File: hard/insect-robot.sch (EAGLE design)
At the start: 9 parts, among them Q1 AO3400, SW1 MK-12C02, U1 ATMEGA328P-QFN32, U2 PW0316

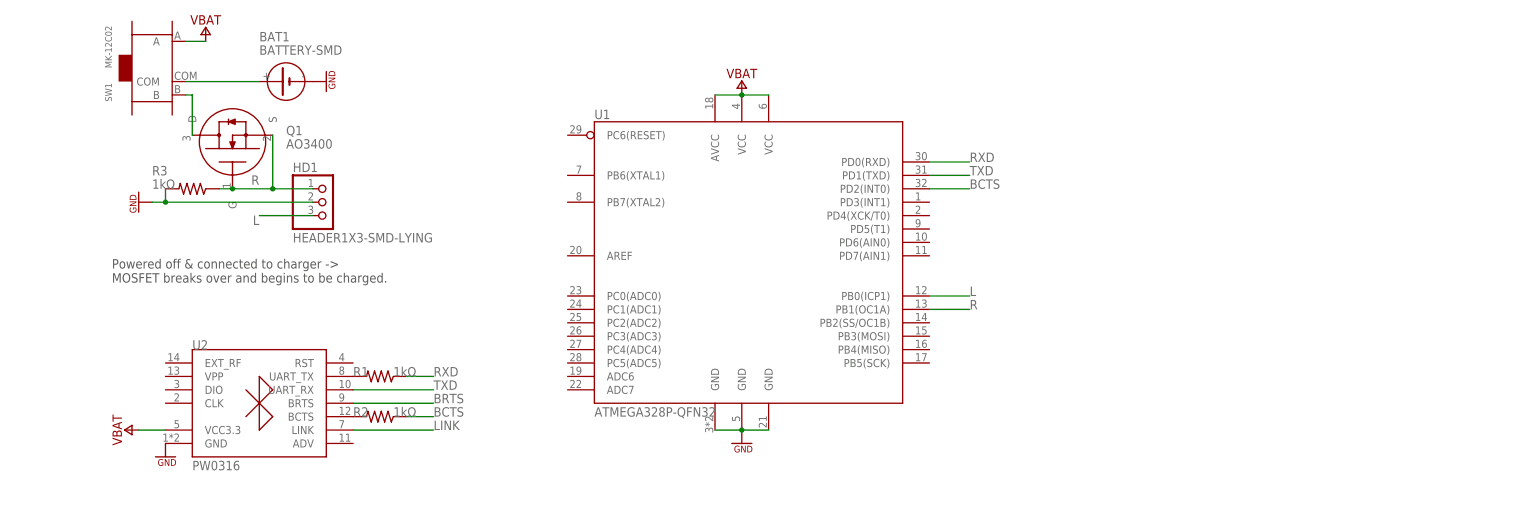
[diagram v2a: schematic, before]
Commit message: Add ISP programming port
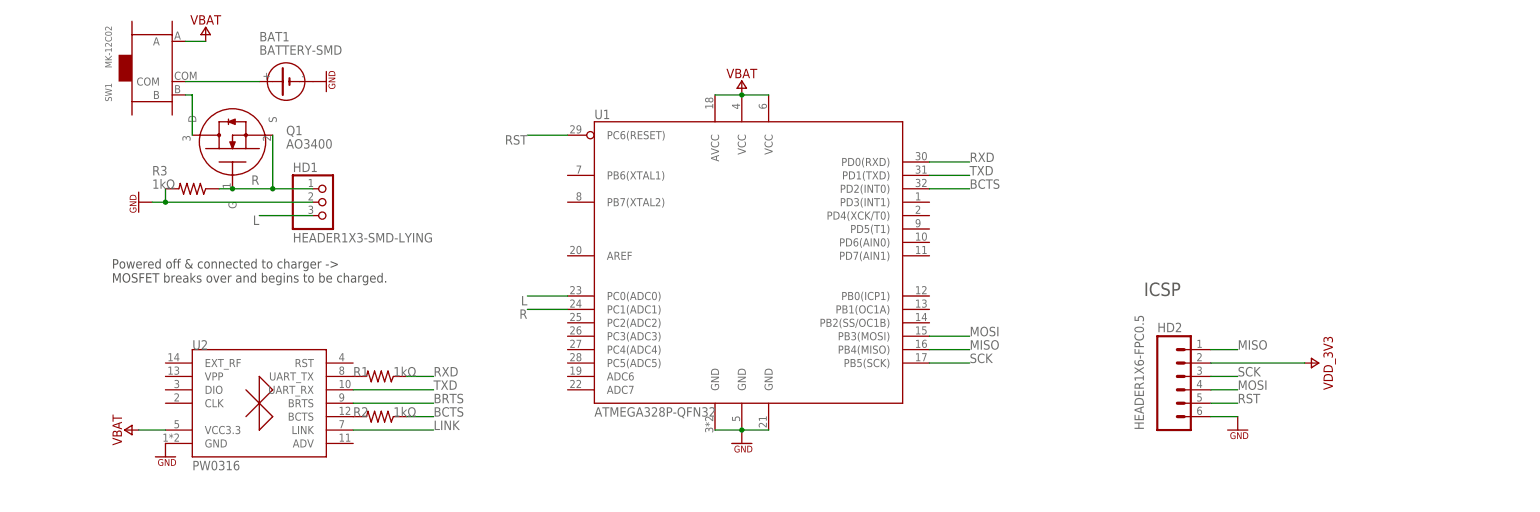
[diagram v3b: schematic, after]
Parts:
- added HD2: HEADER1X6-FPC0.5, MyLibrary:HEADER1X6-FPC0.5
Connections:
- net N$1 renamed SWITCH-B
- new net MISO: HD2.1, U1.PB4(MISO)
- new net MOSI: HD2.4, U1.PB3(MOSI)
- new net RST: HD2.5, U1.PC6(RESET)
- new net SCK: HD2.3, U1.PB5(SCK)
- new net VDD_3V3: HD2.2
- net GND: now also HD2.6
- net L: now also U1.PC0(ADC0); no longer U1.PB0(ICP1)
- net R: now also U1.PC1(ADC1); no longer U1.PB1(OC1A)
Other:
- note added: "ICSP"
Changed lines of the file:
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@@
 <part name="Q1" library="MyLibrary" deviceset="MOSFET" device="-SOT23" value="AO3400"/>
 <part name="R3" library="MyLibrary" deviceset="RES" device="-0603" value="1kΩ"/>
+<part name="HD2" library="MyLibrary" deviceset="HEADER1X6" device="-FPC0.5"/>
+<part name="SUPPLY25" library="MyLibrary" deviceset="GND" device=""/>
+<part name="SUPPLY26" library="MyLibrary" deviceset="VDD_3V3" device=""/>
 </parts>
 <sheets>
@@
 <text x="-119.38" y="-2.54" size="1.778" layer="97">Powered off &amp; connected to charger -&gt;
 MOSFET breaks over and begins to be charged.</text>
+<text x="76.2" y="-5.08" size="2.54" layer="97" font="vector">ICSP</text>
 </plain>
 <instances>
@@
 <attribute name="VALUE" x="-111.76" y="15.24" size="1.778" layer="96"/>
 </instance>
+<instance part="HD2" gate="A" x="83.82" y="-22.86" smashed="yes">
+<attribute name="VALUE" x="76.2" y="-30.48" size="1.778" layer="96" rot="R90"/>
+<attribute name="NAME" x="78.74" y="-11.938" size="1.778" layer="95"/>
+</instance>
+<instance part="SUPPLY25" gate="GND" x="93.98" y="-30.48"/>
+<instance part="SUPPLY26" gate="VDD_3V3" x="109.22" y="-17.78" rot="R270"/>
 </instances>
 <busses>
@@
 <pinref part="U2" gate="P" pin="GND"/>
 <pinref part="SUPPLY7" gate="GND" pin="GND"/>
+</segment>
+<segment>
+<pinref part="HD2" gate="A" pin="6"/>
+<wire x1="88.9" y1="-27.94" x2="93.98" y2="-27.94" width="0.1524" layer="91"/>
+<pinref part="SUPPLY25" gate="GND" pin="GND"/>
 </segment>
 </net>
@@
 </segment>
 <segment>
-<pinref part="U1" gate="P" pin="PB1(OC1A)"/>
-<wire x1="35.56" y1="-7.62" x2="43.18" y2="-7.62" width="0.1524" layer="91"/>
-<label x="43.18" y="-7.62" size="1.778" layer="95" font="vector"/>
+<pinref part="U1" gate="P" pin="PC1(ADC1)"/>
+<wire x1="-33.02" y1="-7.62" x2="-40.64" y2="-7.62" width="0.1524" layer="91"/>
+<label x="-40.64" y="-7.62" size="1.778" layer="95" font="vector" rot="R180"/>
 </segment>
 </net>
@@
 </segment>
 <segment>
-<pinref part="U1" gate="P" pin="PB0(ICP1)"/>
-<wire x1="35.56" y1="-5.08" x2="43.18" y2="-5.08" width="0.1524" layer="91"/>
-<label x="43.18" y="-5.08" size="1.778" layer="95" font="vector"/>
+<pinref part="U1" gate="P" pin="PC0(ADC0)"/>
+<wire x1="-33.02" y1="-5.08" x2="-40.64" y2="-5.08" width="0.1524" layer="91"/>
+<label x="-40.64" y="-5.08" size="1.778" layer="95" font="vector" rot="R180"/>
 </segment>
 </net>
@@
 </segment>
 </net>
-<net name="N$1" class="0">
+<net name="SWITCH-B" class="0">
 <segment>
 <pinref part="Q1" gate="A" pin="D"/>
@@
 </segment>
 </net>
+<net name="MOSI" class="0">
+<segment>
+<pinref part="U1" gate="P" pin="PB3(MOSI)"/>
+<wire x1="35.56" y1="-12.7" x2="43.18" y2="-12.7" width="0.1524" layer="91"/>
+<label x="43.18" y="-12.7" size="1.778" layer="95" font="vector"/>
+</segment>
+<segment>
+<pinref part="HD2" gate="A" pin="4"/>
+<wire x1="88.9" y1="-22.86" x2="93.98" y2="-22.86" width="0.1524" layer="91"/>
+<label x="93.98" y="-22.86" size="1.778" layer="95" font="vector"/>
+</segment>
+</net>
+<net name="MISO" class="0">
+<segment>
+<pinref part="U1" gate="P" pin="PB4(MISO)"/>
+<wire x1="35.56" y1="-15.24" x2="43.18" y2="-15.24" width="0.1524" layer="91"/>
+<label x="43.18" y="-15.24" size="1.778" layer="95" font="vector"/>
+</segment>
+<segment>
+<pinref part="HD2" gate="A" pin="1"/>
+<wire x1="88.9" y1="-15.24" x2="93.98" y2="-15.24" width="0.1524" layer="91"/>
+<label x="93.98" y="-15.24" size="1.778" layer="95" font="vector"/>
+</segment>
+</net>
+<net name="SCK" class="0">
+<segment>
+<pinref part="U1" gate="P" pin="PB5(SCK)"/>
+<wire x1="35.56" y1="-17.78" x2="43.18" y2="-17.78" width="0.1524" layer="91"/>
+<label x="43.18" y="-17.78" size="1.778" layer="95" font="vector"/>
+</segment>
+<segment>
+<pinref part="HD2" gate="A" pin="3"/>
+<wire x1="88.9" y1="-20.32" x2="93.98" y2="-20.32" width="0.1524" layer="91"/>
+<label x="93.98" y="-20.32" size="1.778" layer="95" font="vector"/>
+</segment>
+</net>
+<net name="RST" class="0">
+<segment>
+<pinref part="U1" gate="P" pin="PC6(RESET)"/>
+<wire x1="-33.02" y1="25.4" x2="-40.64" y2="25.4" width="0.1524" layer="91"/>
+<label x="-40.64" y="25.4" size="1.778" layer="95" font="vector" rot="R180"/>
+</segment>
+<segment>
+<pinref part="HD2" gate="A" pin="5"/>
+<wire x1="88.9" y1="-25.4" x2="93.98" y2="-25.4" width="0.1524" layer="91"/>
+<label x="93.98" y="-25.4" size="1.778" layer="95" font="vector"/>
+</segment>
+</net>
+<net name="VDD_3V3" class="0">
+<segment>
+<pinref part="HD2" gate="A" pin="2"/>
+<pinref part="SUPPLY26" gate="VDD_3V3" pin="VDD_3V3"/>
+<wire x1="88.9" y1="-17.78" x2="106.68" y2="-17.78" width="0.1524" layer="91"/>
+</segment>
+</net>

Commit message: Add RGB LED
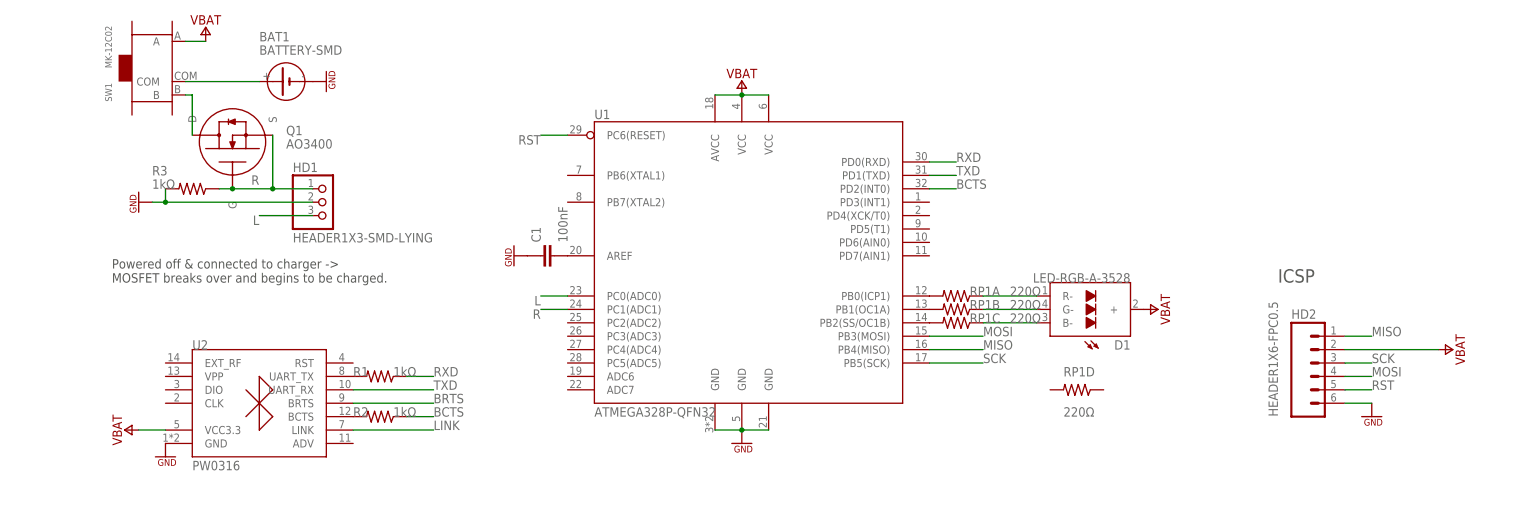
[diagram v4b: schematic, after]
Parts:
- added C1: 100nF, MyLibrary:CAP-0603
- added D1: LED-RGB-A-3528, MyLibrary:LED-RGB-A-3528
- added RP1: 220Ω, MyLibrary:RP-0603
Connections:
- removed net VDD_3V3: HD2.2
- new net N$1: RP1A.2, U1.PB0(ICP1)
- new net N$2: RP1B.2, U1.PB1(OC1A)
- new net N$3: RP1C.2, U1.PB2(SS/OC1B)
- new net N$4: D1.R-, RP1A.1
- new net N$5: D1.G-, RP1B.1
- new net N$6: D1.B-, RP1C.1
- new net N$7: C1.2, U1.AREF
- net GND: now also C1.1
- net VBAT: now also D1.+, HD2.2
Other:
- moved on the sheet: HD2

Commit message: Connect pins
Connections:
- net BRTS: now also U1.PD4(XCK/T0)
- net LINK: now also U1.PD3(INT1)
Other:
- note added: "BRTS: wake the SLAVE up. BCTS: wake the MASTER up."
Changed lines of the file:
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@@
 <sheet>
 <plain>
-<text x="-119.38" y="-2.54" size="1.778" layer="97">Powered off &amp; connected to charger -&gt;
+<text x="-116.84" y="0" size="1.27" layer="97" font="vector">Powered off &amp; connected to charger -&gt;
 MOSFET breaks over and begins to be charged.</text>
 <text x="101.6" y="-2.54" size="2.54" layer="97" font="vector">ICSP</text>
+<text x="-111.76" y="-43.18" size="1.27" layer="97" font="vector">BRTS: wake the SLAVE up.
+BCTS: wake the MASTER up.</text>
 </plain>
 <instances>
@@
 <label x="-58.42" y="-25.4" size="1.778" layer="95" font="vector"/>
 </segment>
+<segment>
+<pinref part="U1" gate="P" pin="PD4(XCK/T0)"/>
+<wire x1="35.56" y1="10.16" x2="40.64" y2="10.16" width="0.1524" layer="91"/>
+<label x="40.64" y="10.16" size="1.778" layer="95" font="vector"/>
+</segment>
 </net>
 <net name="R-BCTS" class="0">
@@
 <label x="-58.42" y="-30.48" size="1.778" layer="95" font="vector"/>
 </segment>
-</net>
+<segment>
+<pinref part="U1" gate="P" pin="PD3(INT1)"/>
+<wire x1="35.56" y1="12.7" x2="40.64" y2="12.7" width="0.1524" layer="91"/>
+<label x="40.64" y="12.7" size="1.778" layer="95" font="vector"/>
+</segment>
+</net>

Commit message: Place the components
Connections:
- net N$1 renamed RR-
- net N$2 renamed RG-
- net N$3 renamed RB-
- net N$4 renamed R-
- net N$5 renamed G-
- net N$6 renamed B-
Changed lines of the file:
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@@
 </segment>
 </net>
-<net name="N$4" class="0">
+<net name="R-" class="0">
 <segment>
 <pinref part="D1" gate="A" pin="R-"/>
@@
 </segment>
 </net>
-<net name="N$5" class="0">
+<net name="G-" class="0">
 <segment>
 <pinref part="D1" gate="A" pin="G-"/>
@@
 </segment>
 </net>
-<net name="N$6" class="0">
+<net name="B-" class="0">
 <segment>
 <pinref part="D1" gate="A" pin="B-"/>
@@
 </segment>
 </net>
-<net name="N$1" class="0">
+<net name="RR-" class="0">
 <segment>
 <pinref part="U1" gate="P" pin="PB0(ICP1)"/>
@@
 </segment>
 </net>
-<net name="N$2" class="0">
+<net name="RG-" class="0">
 <segment>
 <pinref part="U1" gate="P" pin="PB1(OC1A)"/>
@@
 </segment>
 </net>
-<net name="N$3" class="0">
+<net name="RB-" class="0">
 <segment>
 <pinref part="U1" gate="P" pin="PB2(SS/OC1B)"/>

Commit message: Place components
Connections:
- net N$7 renamed AREF
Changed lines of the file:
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@@
 </segment>
 </net>
-<net name="N$7" class="0">
+<net name="AREF" class="0">
 <segment>
 <pinref part="U1" gate="P" pin="AREF"/>

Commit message: Redraw some components
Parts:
- HD2: value HEADER1X6-FPC0.5 -> HEADER1X6-SS-FPC0.5-DRAWER; device MyLibrary:HEADER1X6-FPC0.5 -> MyLibrary:HEADER1X6-SS-FPC0.5-DRAWER
- SW1: value MK-12C02 -> SWITCH-DT; device Seeed-OPL-Button:SMD-TOGGLE-SWITCH-ON-ON(3+4P-6.7X2.7MM) -> MyLibrary:SWITCH-DT
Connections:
- net GND: now also HD2.7, SW1.SS
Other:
- moved on the sheet: BAT1
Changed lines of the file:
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@@
 <setting verticaltext="up"/>
 </settings>
-<grid distance="0.1" unitdist="inch" unit="inch" style="lines" multiple="1" display="no" altdistance="0.01" altunitdist="inch" altunit="inch"/>
+<grid distance="0.1" unitdist="inch" unit="inch" style="lines" multiple="1" display="yes" altdistance="0.01" altunitdist="inch" altunit="inch"/>
 <layers>
 <layer number="1" name="Top" color="4" fill="1" visible="no" active="no"/>
@@
 <part name="SUPPLY1" library="MyLibrary" deviceset="VBAT" device=""/>
 <part name="SUPPLY2" library="MyLibrary" deviceset="GND" device=""/>
-<part name="SW1" library="Seeed-OPL-Button" deviceset="SMD-TOGGLE-SWITCH-ON-ON(3+4P-6.7X2.7MM)" device="" value="MK-12C02"/>
 <part name="BAT1" library="MyLibrary" deviceset="BATTERY" device="-SMD"/>
 <part name="SUPPLY3" library="MyLibrary" deviceset="VBAT" device=""/>
@@
 <part name="Q1" library="MyLibrary" deviceset="MOSFET" device="-SOT23" value="AO3400"/>
 <part name="R3" library="MyLibrary" deviceset="RES" device="-0603" value="1kΩ"/>
-<part name="HD2" library="MyLibrary" deviceset="HEADER1X6" device="-FPC0.5"/>
 <part name="SUPPLY25" library="MyLibrary" deviceset="GND" device=""/>
 <part name="D1" library="MyLibrary" deviceset="LED-RGB-A" device="-3528"/>
@@
 <part name="SUPPLY10" library="MyLibrary" deviceset="GND" device=""/>
 <part name="RP1" library="MyLibrary" deviceset="RP" device="-0603" value="220Ω"/>
+<part name="SUPPLY11" library="MyLibrary" deviceset="GND" device=""/>
+<part name="HD2" library="MyLibrary" deviceset="HEADER1X6-SS" device="-FPC0.5-DRAWER"/>
+<part name="SW1" library="MyLibrary" deviceset="SWITCH-DT" device=""/>
 </parts>
 <sheets>
@@
 <instance part="SUPPLY1" gate="VBAT" x="0" y="35.56"/>
 <instance part="SUPPLY2" gate="GND" x="0" y="-33.02"/>
-<instance part="SW1" gate="G$1" x="-111.76" y="38.1"/>
-<instance part="BAT1" gate="A" x="-86.36" y="35.56" smashed="yes" rot="R180">
-<attribute name="NAME" x="-91.44" y="43.18" size="1.778" layer="95"/>
-<attribute name="VALUE" x="-91.44" y="40.64" size="1.778" layer="96"/>
-</instance>
-<instance part="SUPPLY3" gate="VBAT" x="-101.6" y="45.72"/>
-<instance part="SUPPLY4" gate="GND" x="-78.74" y="35.56" rot="R90"/>
+<instance part="BAT1" gate="A" x="-124.46" y="35.56" smashed="yes">
+<attribute name="NAME" x="-119.38" y="27.94" size="1.778" layer="95" rot="R180"/>
+<attribute name="VALUE" x="-119.38" y="30.48" size="1.778" layer="96" rot="R180"/>
+</instance>
+<instance part="SUPPLY3" gate="VBAT" x="-99.06" y="40.64"/>
+<instance part="SUPPLY4" gate="GND" x="-132.08" y="35.56" rot="R270"/>
 <instance part="HD1" gate="A" x="-78.74" y="12.7"/>
 <instance part="SUPPLY5" gate="GND" x="-114.3" y="12.7" rot="R270"/>
@@
 <attribute name="VALUE" x="-111.76" y="15.24" size="1.778" layer="96"/>
 </instance>
-<instance part="HD2" gate="A" x="109.22" y="-20.32" smashed="yes">
-<attribute name="VALUE" x="101.6" y="-27.94" size="1.778" layer="96" rot="R90"/>
-<attribute name="NAME" x="104.14" y="-9.398" size="1.778" layer="95"/>
-</instance>
-<instance part="SUPPLY25" gate="GND" x="119.38" y="-27.94"/>
+<instance part="SUPPLY25" gate="GND" x="134.62" y="-27.94" rot="R90"/>
 <instance part="D1" gate="A" x="66.04" y="-7.62" rot="MR270"/>
 <instance part="SUPPLY9" gate="VBAT" x="134.62" y="-15.24" rot="R270"/>
@@
 </instance>
 <instance part="RP1" gate="D" x="63.5" y="-22.86"/>
+<instance part="SUPPLY11" gate="GND" x="-111.76" y="27.94"/>
+<instance part="HD2" gate="A" x="109.22" y="-20.32"/>
+<instance part="SW1" gate="A" x="-109.22" y="35.56" rot="MR0"/>
 </instances>
 <busses>
@@
 </segment>
 <segment>
-<pinref part="SUPPLY3" gate="VBAT" pin="VBAT"/>
-<pinref part="SW1" gate="G$1" pin="A"/>
-<wire x1="-101.6" y1="43.18" x2="-105.41" y2="43.18" width="0.1524" layer="91"/>
-</segment>
-<segment>
-<pinref part="HD2" gate="A" pin="2"/>
 <wire x1="114.3" y1="-15.24" x2="132.08" y2="-15.24" width="0.1524" layer="91"/>
 <pinref part="SUPPLY9" gate="VBAT" pin="VBAT"/>
+<pinref part="HD2" gate="A" pin="2"/>
 </segment>
 <segment>
 <pinref part="D1" gate="A" pin="+"/>
 <pinref part="SUPPLY8" gate="VBAT" pin="VBAT"/>
+</segment>
+<segment>
+<pinref part="SUPPLY3" gate="VBAT" pin="VBAT"/>
+<pinref part="SW1" gate="A" pin="A"/>
+<wire x1="-99.06" y1="38.1" x2="-104.14" y2="38.1" width="0.1524" layer="91"/>
 </segment>
 </net>
@@
 </segment>
 <segment>
-<pinref part="HD2" gate="A" pin="6"/>
-<wire x1="114.3" y1="-25.4" x2="119.38" y2="-25.4" width="0.1524" layer="91"/>
-<pinref part="SUPPLY25" gate="GND" pin="GND"/>
-</segment>
-<segment>
 <pinref part="C1" gate="A" pin="1"/>
 <pinref part="SUPPLY10" gate="GND" pin="GND"/>
 </segment>
-</net>
-<net name="BAT-COM" class="0">
-<segment>
-<pinref part="BAT1" gate="A" pin="+"/>
-<pinref part="SW1" gate="G$1" pin="COM"/>
-<wire x1="-91.44" y1="35.56" x2="-105.41" y2="35.56" width="0.1524" layer="91"/>
+<segment>
+<pinref part="HD2" gate="A" pin="7"/>
+<pinref part="SUPPLY25" gate="GND" pin="GND"/>
+<wire x1="114.3" y1="-27.94" x2="119.38" y2="-27.94" width="0.1524" layer="91"/>
+<pinref part="HD2" gate="A" pin="6"/>
+<wire x1="119.38" y1="-27.94" x2="132.08" y2="-27.94" width="0.1524" layer="91"/>
+<wire x1="114.3" y1="-25.4" x2="119.38" y2="-25.4" width="0.1524" layer="91"/>
+<wire x1="119.38" y1="-25.4" x2="119.38" y2="-27.94" width="0.1524" layer="91"/>
+<junction x="119.38" y="-27.94"/>
+</segment>
+<segment>
+<pinref part="SW1" gate="A" pin="SS"/>
+<wire x1="-111.76" y1="33.02" x2="-111.76" y2="30.48" width="0.1524" layer="91"/>
+<pinref part="SUPPLY11" gate="GND" pin="GND"/>
 </segment>
 </net>
@@
 <pinref part="Q1" gate="A" pin="D"/>
 <wire x1="-104.14" y1="25.4" x2="-104.14" y2="33.02" width="0.1524" layer="91"/>
-<pinref part="SW1" gate="G$1" pin="B"/>
-<wire x1="-104.14" y1="33.02" x2="-105.41" y2="33.02" width="0.1524" layer="91"/>
+<pinref part="SW1" gate="A" pin="B"/>
 </segment>
 </net>
@@
 </segment>
 <segment>
-<pinref part="HD2" gate="A" pin="4"/>
 <wire x1="114.3" y1="-20.32" x2="119.38" y2="-20.32" width="0.1524" layer="91"/>
 <label x="119.38" y="-20.32" size="1.778" layer="95" font="vector"/>
+<pinref part="HD2" gate="A" pin="4"/>
 </segment>
 </net>
@@
 </segment>
 <segment>
-<pinref part="HD2" gate="A" pin="1"/>
 <wire x1="114.3" y1="-12.7" x2="119.38" y2="-12.7" width="0.1524" layer="91"/>
 <label x="119.38" y="-12.7" size="1.778" layer="95" font="vector"/>
+<pinref part="HD2" gate="A" pin="1"/>
 </segment>
 </net>
@@
 </segment>
 <segment>
-<pinref part="HD2" gate="A" pin="3"/>
 <wire x1="114.3" y1="-17.78" x2="119.38" y2="-17.78" width="0.1524" layer="91"/>
 <label x="119.38" y="-17.78" size="1.778" layer="95" font="vector"/>
+<pinref part="HD2" gate="A" pin="3"/>
 </segment>
 </net>
@@
 </segment>
 <segment>
-<pinref part="HD2" gate="A" pin="5"/>
 <wire x1="114.3" y1="-22.86" x2="119.38" y2="-22.86" width="0.1524" layer="91"/>
 <label x="119.38" y="-22.86" size="1.778" layer="95" font="vector"/>
+<pinref part="HD2" gate="A" pin="5"/>
 </segment>
 </net>
@@
 </segment>
 </net>
+<net name="BAT-COM" class="0">
+<segment>
+<pinref part="BAT1" gate="A" pin="+"/>
+<pinref part="SW1" gate="A" pin="COM"/>
+<wire x1="-119.38" y1="35.56" x2="-114.3" y2="35.56" width="0.1524" layer="91"/>
+</segment>
+</net>
 </nets>
 </sheet>
 </sheets>
+<errors>
+</errors>
 </schematic>
 </drawing>
